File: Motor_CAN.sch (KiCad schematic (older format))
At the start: 18 parts, among them J19 CAN_OUT, J20 MotorCANConnector, J27 CAN_TP, U14 ADM3055E, U15 CDSOT23-T24CAN

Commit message: Organizes the schematic into hierarchical sheets
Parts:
- J20: Digikey (none) -> https://www.digikey.com/product-detail/en/te-connectivity-a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
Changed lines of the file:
@@
 $Descr A4 11693 8268
 encoding utf-8
-Sheet 5 5
+Sheet 5 10
 Title ""
 Date ""
@@
 F 2 "UTSVT_Connectors:TE_4-2172079-2" H 9200 5150 50  0001 C CNN
 F 3 "" H 9200 5150 50  0001 C CNN
+F 4 "https://www.digikey.com/product-detail/en/te-connectivity-amp-connectors/4-2172079-2/A120861-ND/5118755" H 9200 5150 50  0001 C CNN "Digikey"
 	1    9200 5150
 	-1   0    0    -1

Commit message: removes the isp
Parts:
- J20: symbol utsvt-connectors:MotorCANConnector -> Dashboard-rescue:MotorCANConnector-utsvt-connectors
- U14: symbol utsvt-chips:ADM3055E -> Dashboard-rescue:ADM3055E-utsvt-chips
- U15: symbol utsvt-chips:CDSOT23-T24CAN -> Dashboard-rescue:CDSOT23-T24CAN-utsvt-chips
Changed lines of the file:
@@
 $EndComp
 $Comp
-L utsvt-chips:ADM3055E U?
+L Dashboard-rescue:ADM3055E-utsvt-chips U?
 U 1 1 5F63A68F
 P 4300 3750
@@
 $EndComp
 $Comp
-L utsvt-chips:CDSOT23-T24CAN U?
+L Dashboard-rescue:CDSOT23-T24CAN-utsvt-chips U?
 U 1 1 5F63A696
 P 8050 3000
@@
 	8650 3300 8650 3900
 $Comp
-L utsvt-connectors:MotorCANConnector J20
+L Dashboard-rescue:MotorCANConnector-utsvt-connectors J20
 U 1 1 5F63ED37
 P 9200 5150

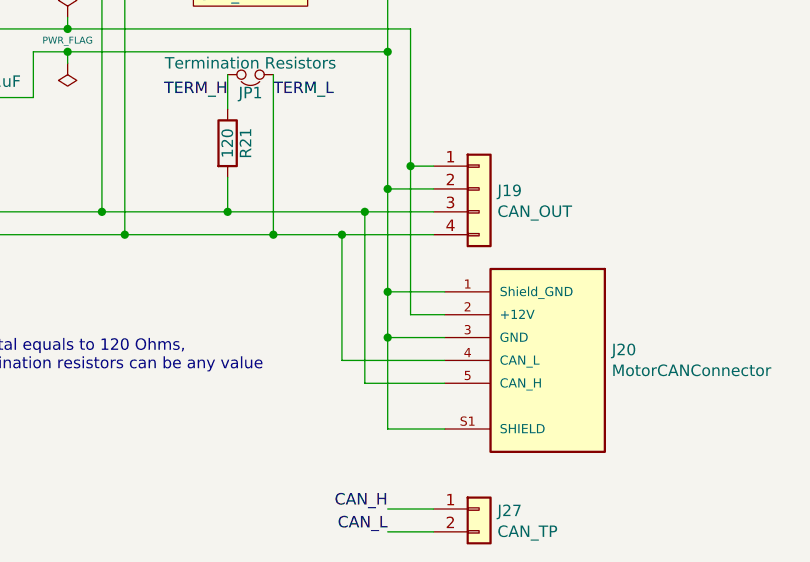
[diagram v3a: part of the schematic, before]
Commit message: Changes the layout of the board, adds resistors for ignition switch, and gives motar can isolated +12v, still need to change resistor value for the isolated +12v(didnt remember how to find the value)
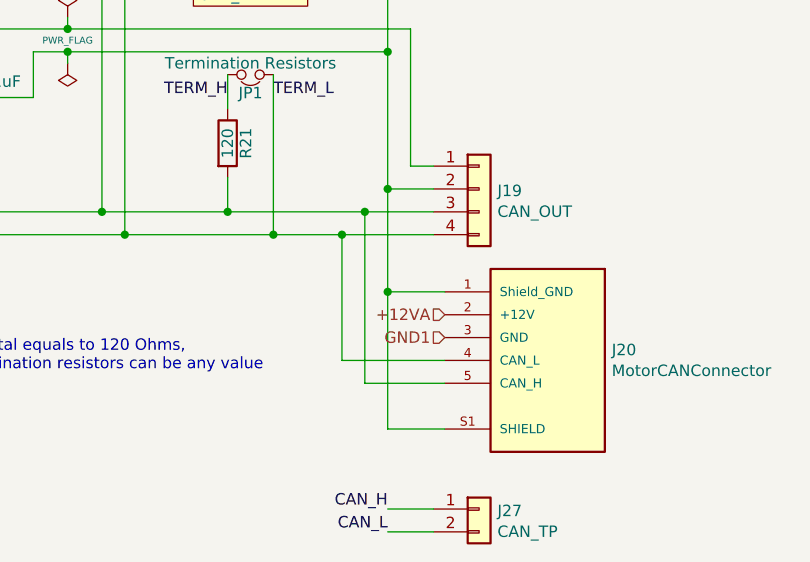
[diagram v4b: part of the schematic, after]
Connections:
- net at C28.1, C29.1, C30.1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: no longer J20.2 (+12V)
- net at C28.2, C29.2, C30.2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: no longer J20.3 (GND)
- new net +12VA: J20.2 (+12V)
- new net GND1: J20.3 (GND)
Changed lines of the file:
@@
 $Descr A4 11693 8268
 encoding utf-8
-Sheet 4 10
+Sheet 10 10
 Title ""
 Date ""
@@
 	8150 4100 8450 4100
 Wire Wire Line
-	8750 3800 8750 4450
-Wire Wire Line
-	8750 4450 8900 4450
-Connection ~ 8750 3800
-Wire Wire Line
 	8650 3900 8650 4350
-Wire Wire Line
-	8650 4550 8900 4550
 Connection ~ 8650 3900
 Wire Wire Line
@@
 Connection ~ 8650 4350
 Wire Wire Line
-	8650 4350 8650 4550
-Wire Wire Line
-	8650 4550 8650 4950
-Wire Wire Line
 	8650 4950 8900 4950
-Connection ~ 8650 4550
 Wire Wire Line
 	8550 4000 8550 4750
@@
 Wire Wire Line
 	7950 4000 8550 4000
+Wire Wire Line
+	8650 4350 8650 4950
+Text HLabel 8900 4450 0    50   Input ~ 0
++12VA
+Text HLabel 8900 4550 0    50   Input ~ 0
+GND1
 $EndSCHEMATC
